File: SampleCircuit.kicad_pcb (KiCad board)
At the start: 2 copper layers, 101.6 x 101.6 mm, 50 parts, among them J1 24V INPUT, J2 12V TEST, J3 5V TEST, J4 3.3V TEST, J5 SPEAKER, SW1 RESET, SW2 BOOT, U1 LMZM23601SILR, U15 TLV803S, U2 ESP32-S3-WROOM-1, U23 RV-3028-C7, U24 LMZM23601SILR, U25 LMZM23601SILR, U5 NS4168, U6 MicroSD

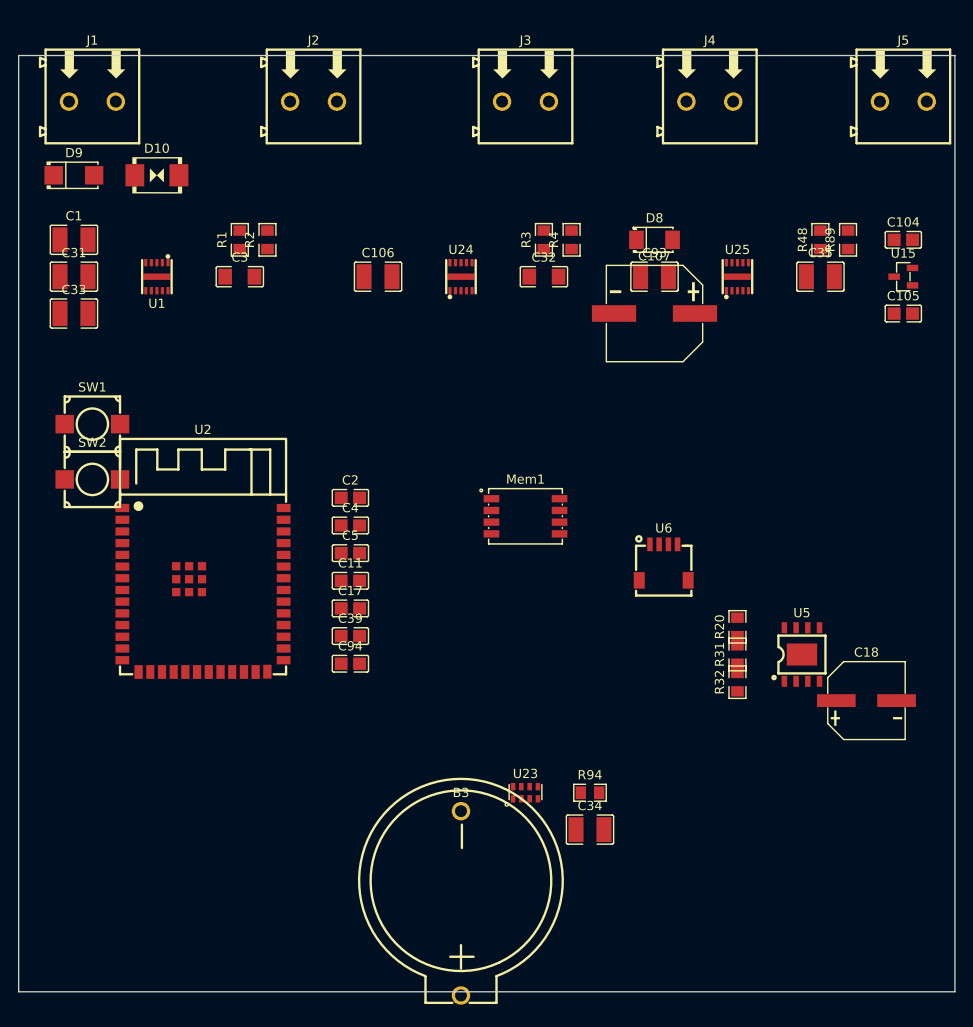
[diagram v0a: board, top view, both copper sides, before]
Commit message: Compact PCB layout and add PCBPlacement spec v1.3
PCB changes:
- Connectors J1-J5 evenly spaced along top edge at same Y offset
- PSU passives compacted within 3mm of their IC pins (12V, 5V, 3.3V)
- R89 moved near U23 (RTC), R48 near U15 (supervisor), R31/R32 near U24
- All components oriented for optimal routing (passives aligned to trace direction)
- Silkscreen refs repositioned to clear all pads with cascading size/rotation
- All value text hidden (ref designators only)

New spec (specs/PCBPlacement.spec v1.3):
- S1e: Connector alignment and even distribution rule
- S3e: Pad-to-pad overlap prevention
- S4f-4i: Compact grouping with dead space acceptable on edges
- S5: RF/antenna rules defer to manufacturer specs (general, not ESP32-specific)
- S9: Silkscreen management with cascading resize/rotate/reposition algorithm
- S9f: Silkscreen-to-silkscreen overlap prevention
- S11: Full verification template with all checks

Board passes all 8 verification checks (50 components, 198 pads, 50 silkscreen refs).

Co-Authored-By: Claude Opus 4.6 <noreply@anthropic.com>
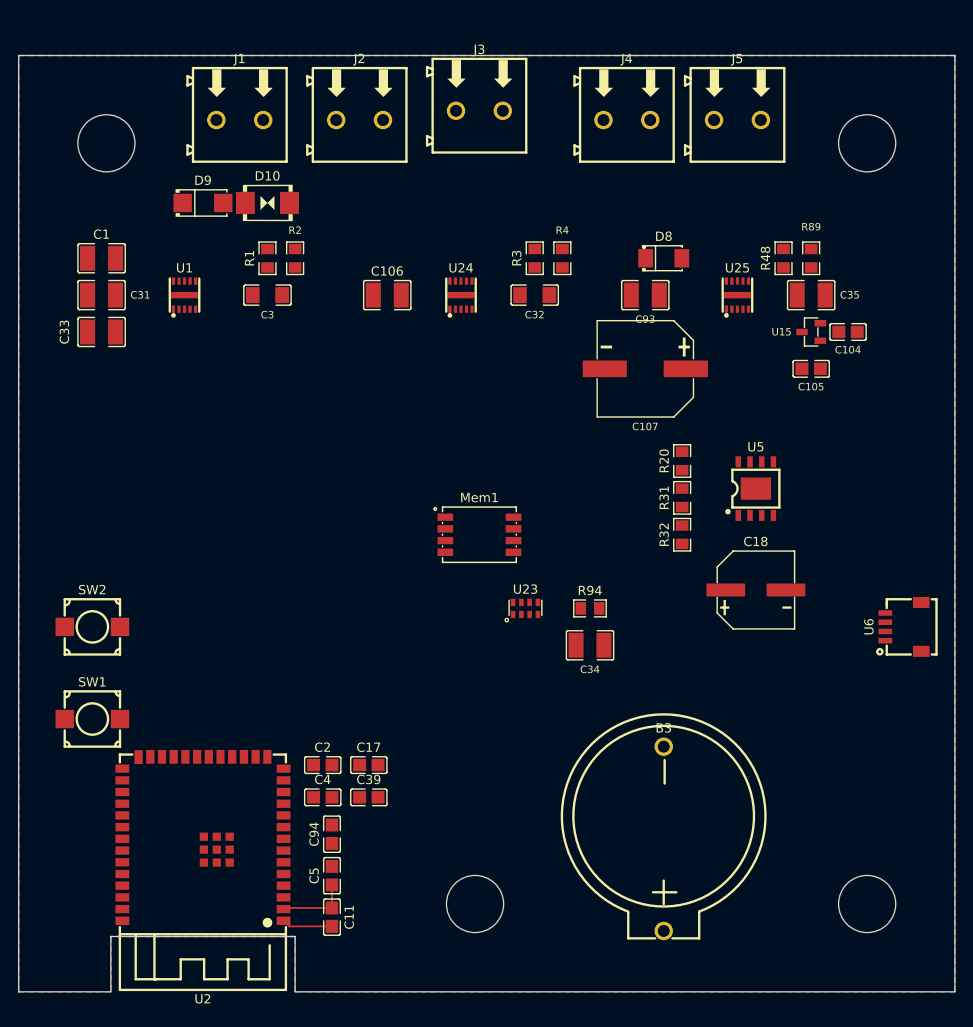
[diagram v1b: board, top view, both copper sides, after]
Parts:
- moved C11 36.6 mm to (134.0, 143.5), turned to -90 degrees
- moved C5 35.1 mm to (134.0, 139.0), turned to 90 degrees
- moved SW1 32.0 mm to (108.0, 122.0)
- moved C4 29.7 mm to (133.0, 130.5)
- moved C2 29.2 mm to (133.0, 127.0)
- moved U2 27.0 mm to (120.0, 135.0), turned to 180 degrees
- moved U6 26.9 mm to (196.0, 112.0), turned to 90 degrees
- moved B3 23.1 mm to (170.0, 135.0)
- moved C34 20.0 mm to (162.0, 114.0)
- moved R94 20.0 mm to (162.0, 110.0)
- moved U23 20.0 mm to (155.0, 110.0)
- moved R20 19.0 mm to (172.0, 94.0)
- moved U5 18.7 mm to (180.0, 97.0)
- moved C94 18.6 mm to (134.0, 134.5), turned to 90 degrees
- moved J5 18.1 mm to (178.0, 57.0)
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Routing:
- net +3.3V: track 0.00 -> 7.80 mm
- net GND: track 0.00 -> 5.50 mm
- added copper zone on B.Cu, net GND
- added copper zone on F.Cu, net GND
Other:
- outline, holes or cut-outs redrawn

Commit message: Optimize PCB placement: fix violations, align antenna cutout, add spec 6g
- Fix S2: move B3 clear of BR mounting hole, R1 clear of ML hole
- Fix S3: move U5+R20 south to reduce I2S signal distances (51mm→45mm)
- Fix S4: resolve U6/B3 overlap
- Fix S10a: reposition 8 silkscreen refs off pads
- Fix S10f: resolve SW1 silk-on-silk overlaps
- Move antenna cutout from x=108-128 to x=140-160 (aligned with U2)
- Add spec rule 6g: cutout healing when antenna components move
- Result: 0 errors, 7 warnings (all ratsnest <50mm)

Co-Authored-By: Claude Opus 4.6 <noreply@anthropic.com>
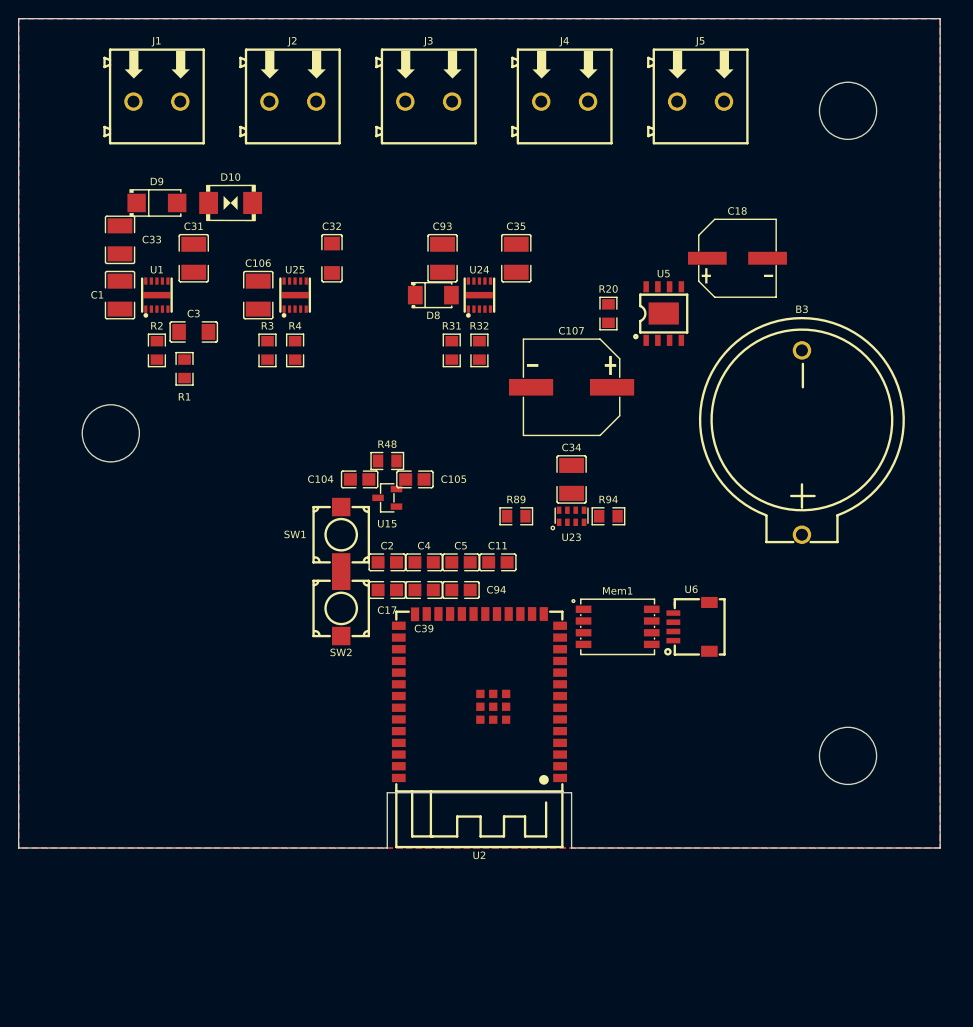
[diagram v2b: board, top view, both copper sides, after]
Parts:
- moved C104 55.4 mm to (137.0, 96.0)
- moved U15 49.4 mm to (140.0, 98.0)
- moved R48 48.3 mm to (140.0, 94.0), turned to 0 degrees
- moved U25 48.0 mm to (130.0, 76.0)
- moved B3 45.5 mm to (185.0, 92.0)
- moved C105 44.6 mm to (143.0, 96.0)
- moved R89 42.5 mm to (154.0, 100.0), turned to 0 degrees
- moved C11 42.5 mm to (152.0, 105.0), turned to 0 degrees
- moved C5 36.8 mm to (148.0, 105.0), turned to 0 degrees
- moved C18 36.1 mm to (178.0, 72.0)
- moved U2 33.8 mm to (150.0, 119.5)
- moved SW1 33.6 mm to (135.0, 102.0), turned to 90 degrees
- moved C35 32.2 mm to (154.0, 72.0), turned to 90 degrees
- moved R3 30.7 mm to (127.0, 82.0)
- moved R4 30.7 mm to (130.0, 82.0)
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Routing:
- net +3.3V: track 7.80 -> 0.00 mm
- net GND: track 5.50 -> 0.00 mm
- removed copper zone on B.Cu, net GND
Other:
- board size 101.6 x 101.6 mm -> 100 x 90 mm

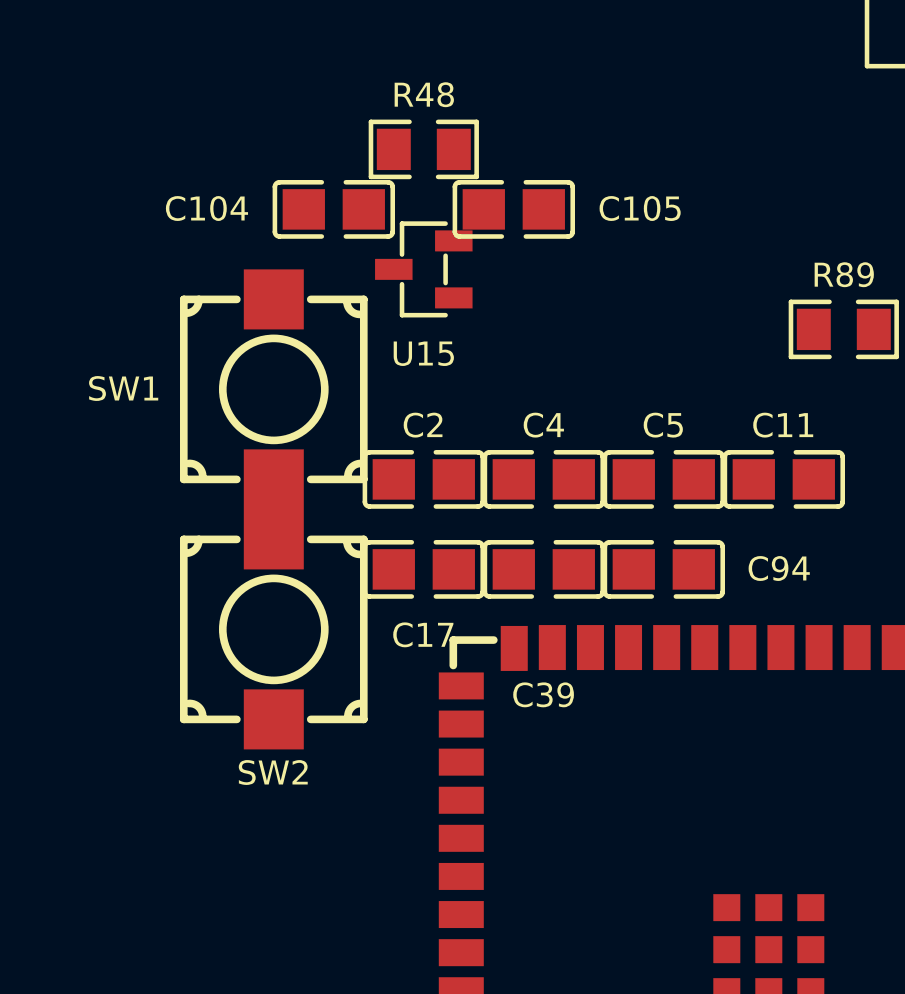
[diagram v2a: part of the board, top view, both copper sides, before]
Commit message: Add spec rule 4g (pad-to-pad clearance) and fix violations
- New rule 4g: 0.20mm minimum pad-to-pad clearance between different
  components to prevent solder bridging (IPC Class 2)
- Fix SW1/SW2 touching pads (0.00mm gap → 0.5mm)
- Fix U15/C105 near-touching pads (0.03mm gap → safe clearance)
- All verification checks now pass (0 errors, 7 warnings)

Co-Authored-By: Claude Opus 4.6 <noreply@anthropic.com>
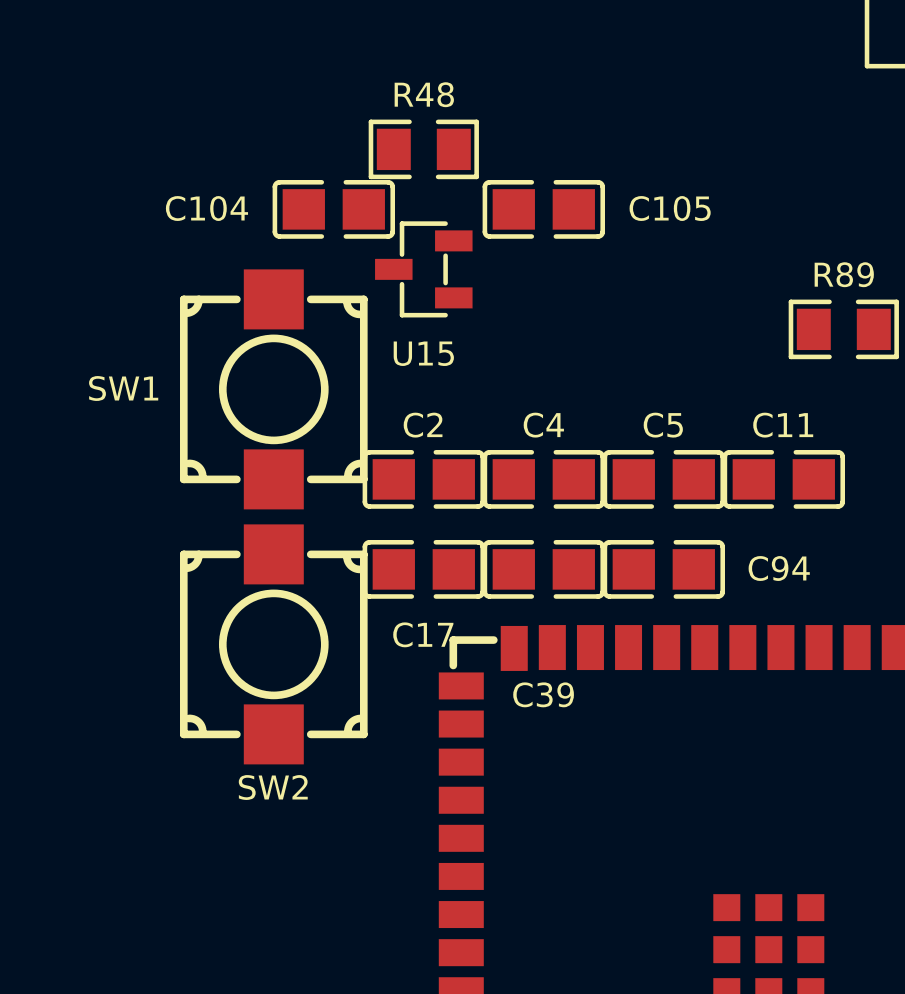
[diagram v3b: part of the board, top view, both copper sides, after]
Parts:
- moved C105 1.00 mm to (144.0, 96.0)
- moved SW2 0.50 mm to (135.0, 110.5)
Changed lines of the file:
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@@
 	(footprint "JLCImport:CL21A106KAYNNNE"
 		(layer "F.Cu")
-		(at 143 96)
+		(at 144 96)
 		(descr "10uF (106) ±10% 25V")
 		(tags "C0805 C15850 CL21A106KAYNNNE SAMSUNG")
@@
 	(footprint "JLCImport:TS665WS_C2686403"
 		(layer "F.Cu")
-		(at 135 110 90)
+		(at 135 110.5 90)
 		(descr "TS665WS; KEY-SMD_L6.0-W6.0-LS6.6; SHOU HAN")
 		(tags "C2686403 KEY-SMD_L6.0-W6.0-LS6.6 SHOU HAN TS665WS")
